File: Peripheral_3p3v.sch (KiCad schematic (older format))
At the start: 0 parts

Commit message: Lots of changes for MFG: parts info
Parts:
- added L3: 4.7uH, symbol Device:L
- added U8: TPS54202HDDCR, SmartBattery:SOT95P280X110-6N, symbol SmartBattery:TPS54202HDDCR
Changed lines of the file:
@@
 $Descr A4 11693 8268
 encoding utf-8
-Sheet 1 5
+Sheet 5 5
 Title ""
 Date ""
@@
 Comment4 ""
 $EndDescr
+$Comp
+L SmartBattery:TPS54202HDDCR U8
+U 1 1 5FE1C5BF
+P 3950 3400
+F 0 "U8" H 3950 3970 50  0000 C CNN
+F 1 "TPS54202HDDCR" H 3950 3879 50  0000 C CNN
+F 2 "SmartBattery:SOT95P280X110-6N" H 3950 3400 50  0001 L BNN
+F 3 "" H 3950 3400 50  0001 L BNN
+F 4 "TPS54202HDDCR" H 3950 3400 50  0001 C CNN "SKU"
+	1    3950 3400
+	1    0    0    -1
+$EndComp
+$Comp
+L Device:L L3
+U 1 1 5FE1E2B4
+P 6100 3350
+F 0 "L3" H 6153 3396 50  0000 L CNN
+F 1 "4.7uH" H 6153 3305 50  0000 L CNN
+F 2 "" H 6100 3350 50  0001 C CNN
+F 3 "~" H 6100 3350 50  0001 C CNN
+F 4 "303010114" H 6100 3350 50  0001 C CNN "SKU"
+	1    6100 3350
+	1    0    0    -1
+$EndComp
 $EndSCHEMATC

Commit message: Switching over to jlpcb
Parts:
- removed U8: TPS54202HDDCR, SmartBattery:SOT95P280X110-6N, symbol SmartBattery:TPS54202HDDCR
- added U8: LMR14030SDDAR, SmartBattery:NOPB, symbol SmartBattery:LMR14030SDDAR
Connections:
- net labels added: 3p3v, VSYS
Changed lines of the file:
@@
 $Descr A4 11693 8268
 encoding utf-8
-Sheet 5 5
+Sheet 5 6
 Title ""
 Date ""
@@
 Comment4 ""
 $EndDescr
-$Comp
-L SmartBattery:TPS54202HDDCR U8
-U 1 1 5FE1C5BF
-P 3950 3400
-F 0 "U8" H 3950 3970 50  0000 C CNN
-F 1 "TPS54202HDDCR" H 3950 3879 50  0000 C CNN
-F 2 "SmartBattery:SOT95P280X110-6N" H 3950 3400 50  0001 L BNN
-F 3 "" H 3950 3400 50  0001 L BNN
-F 4 "TPS54202HDDCR" H 3950 3400 50  0001 C CNN "SKU"
-	1    3950 3400
-	1    0    0    -1
-$EndComp
 $Comp
 L Device:L L3
@@
 	1    0    0    -1
 $EndComp
+$Comp
+L SmartBattery:LMR14030SDDAR U8
+U 1 1 60084A34
+P 3350 3250
+F 0 "U8" H 3350 3920 50  0000 C CNN
+F 1 "LMR14030SDDAR" H 3350 3829 50  0000 C CNN
+F 2 "SmartBattery:NOPB" H 3350 3250 50  0001 L BNN
+F 3 "" H 3350 3250 50  0001 L BNN
+F 4 "C182078" H 3350 3250 50  0001 C CNN "LCSC"
+	1    3350 3250
+	1    0    0    -1
+$EndComp
+Text HLabel 1600 1600 0    50   Input ~ 0
+VSYS
+Text HLabel 5650 1650 2    50   Output ~ 0
+3p3v
 $EndSCHEMATC

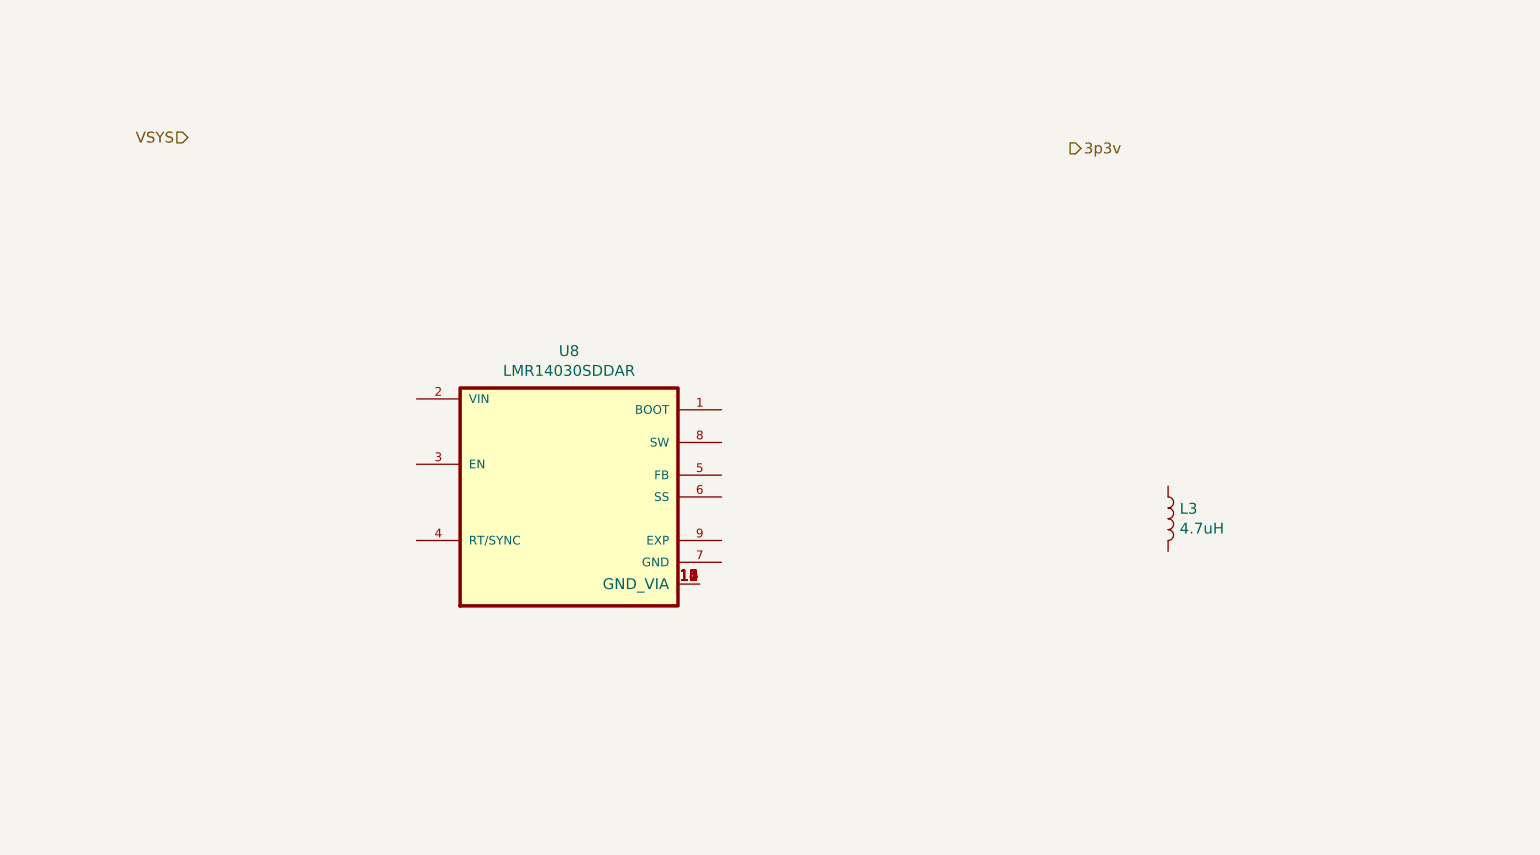
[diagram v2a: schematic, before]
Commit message: Replaced old charger to support JLC assembly. Very close now!
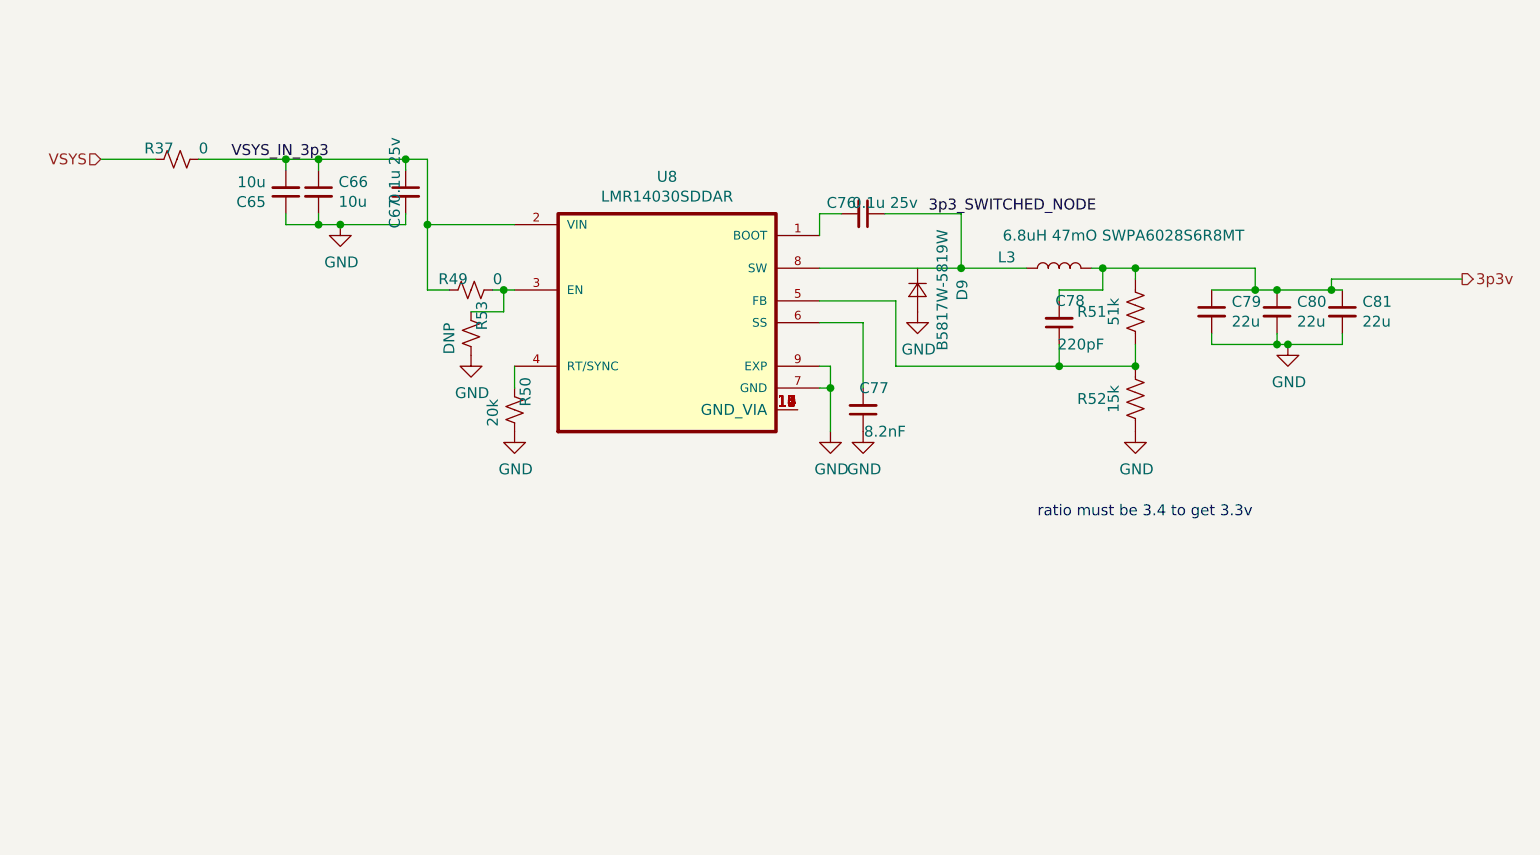
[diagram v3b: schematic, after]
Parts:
- added C65, C66: 10u, lc_lib:0805_C, symbol Device:C_Small
- added C67, C76: 0.1u 25v, lc_lib:0402_C, symbol Device:C_Small
- added C77: 8.2nF, lc_lib:0603_C, symbol Device:C_Small
- added C78: 220pF, lc_lib:0402_C, symbol Device:C_Small
- added C79, C80, C81: 22u, lc_lib:0805_C, symbol Device:C_Small
- added D9: B5817W-5819W, lc_lib:SOD-123, symbol Device:D_Small
- added R37, R49: 0, lc_lib:0402_R, symbol Device:R_Small_US
- added R50: 20k, lc_lib:0402_R, symbol Device:R_Small_US
- added R51: 51k, lc_lib:0402_R, symbol Device:R_US
- added R52: 15k, lc_lib:0402_R, symbol Device:R_US
- added R53: DNP, lc_lib:0402_R, symbol Device:R_Small_US
- L3: value 4.7uH -> 6.8uH 47mO SWPA6028S6R8MT; footprint (none) -> Inductor_SMD:L_Taiyo-Yuden_NR-60xx; SKU 303010114 -> (none); lcsc (none) -> C42261
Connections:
- net 3p3v: now also L3.2, C78.2, C79.1, C80.1, C81.1, R51.1
- net VSYS: now also R37.2
- net 3p3_SWITCHED_NODE: now reaches L3.1
- net 3p3_SWITCHED_NODE: now also U8.8 (SW), C76.1
- net at U8.1 (BOOT): now also C76.2
- net VSYS_IN_3p3: now reaches U8.2 (VIN)
- net VSYS_IN_3p3: now also C65.2, C66.1, C67.1, R37.1, R49.2
- net at U8.3 (EN): now also R49.1, R53.2
- net at U8.4 (RT/SYNC): now also R50.2
- net at U8.5 (FB): now also C78.1, R51.2, R52.1
- net at U8.6 (SS): now also C77.2
- net GND: now reaches U8.7 (GND)
- net GND: now also U8.9 (EXP), C65.1, C66.2, C67.2, C77.1, C79.2, C80.2, C81.2, D9.2 (A), R50.1, R52.2, R53.1
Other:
- note added: "ratio must be 3.4 to get 3.3v\n"
- moved on the sheet: L3, U8

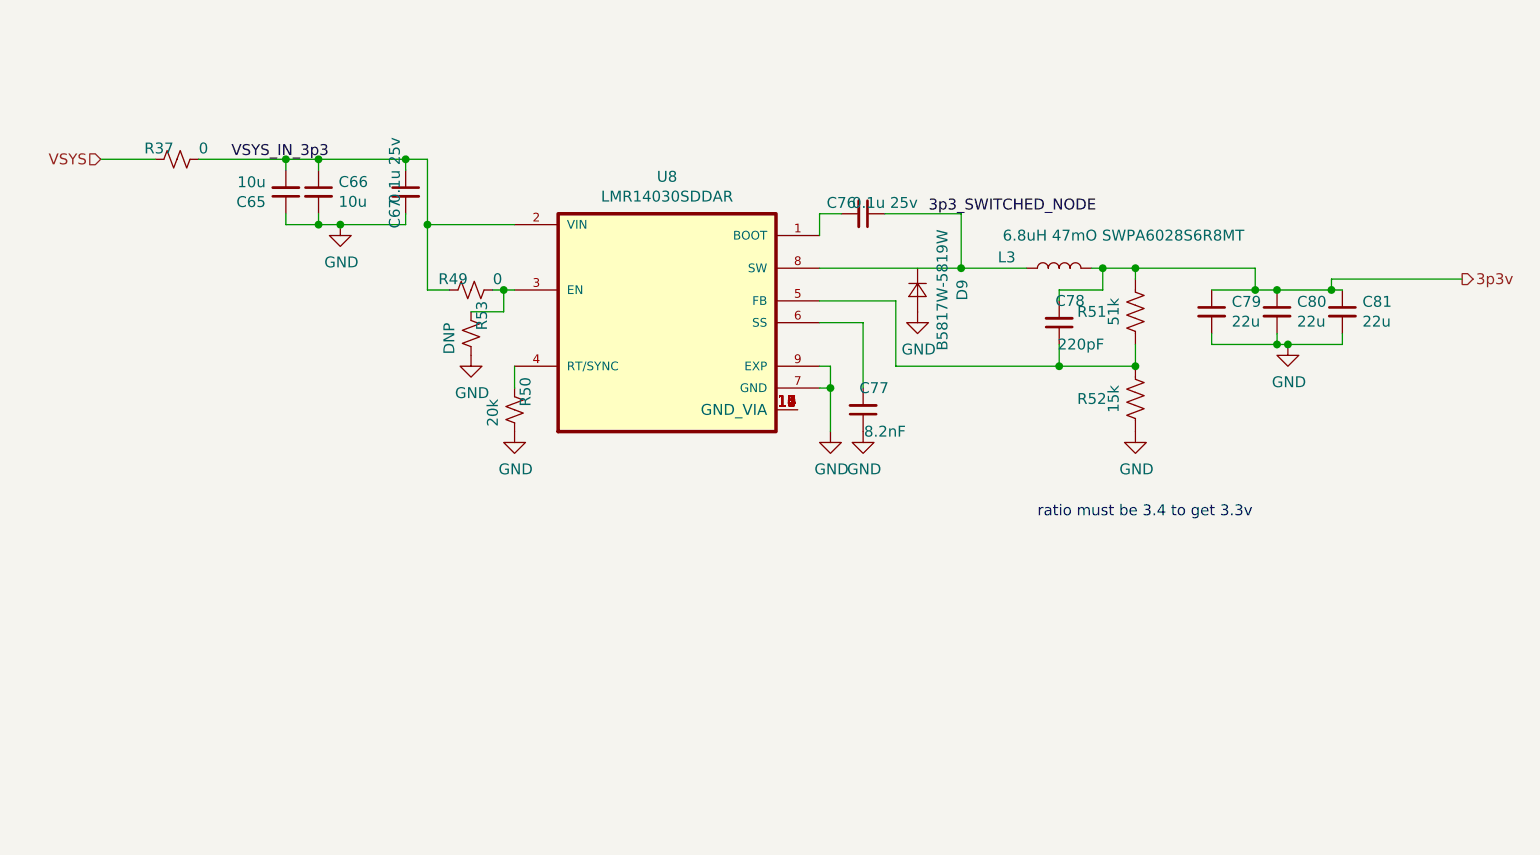
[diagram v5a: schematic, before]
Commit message: Type_A_implemented. Sch "locked". PCB Layout started.
*Changelog:
*Type-a switching regulator (TBD -- need to check inductor,caps, stability. Maybe check both peripherial inductors?)
*Type-A load switch + connector + esd
*started layout..
*found out that my footprint for n fet is wrong. Fixing now, need to replace all of those.
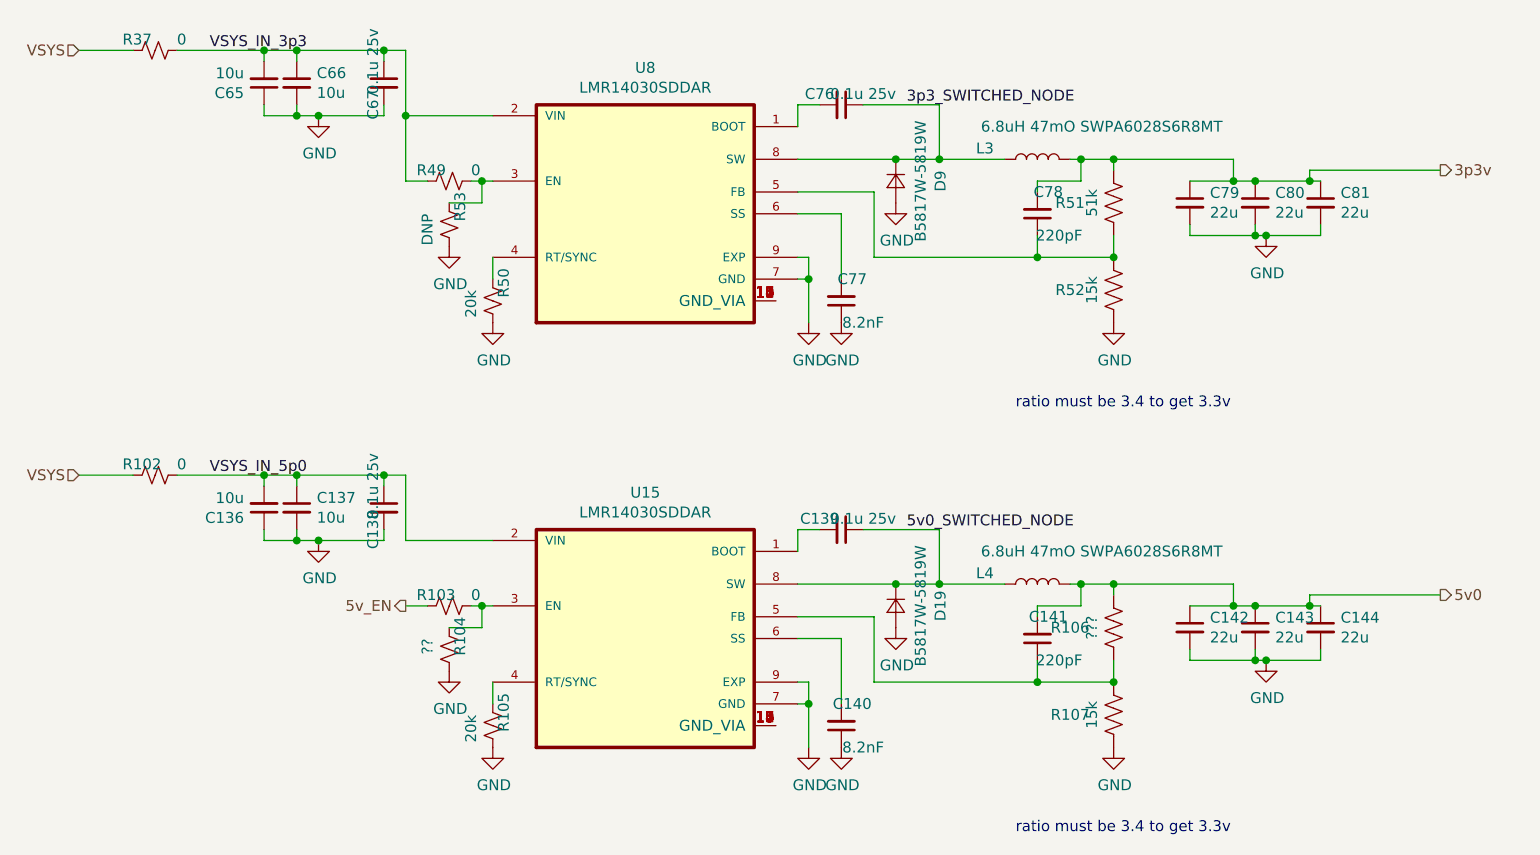
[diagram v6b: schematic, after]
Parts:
- added C136, C137: 10u, lc_lib:0805_C, symbol Device:C_Small
- added C138, C139: 0.1u 25v, lc_lib:0402_C, symbol Device:C_Small
- added C140: 8.2nF, lc_lib:0603_C, symbol Device:C_Small
- added C141: 220pF, lc_lib:0402_C, symbol Device:C_Small
- added C142, C143, C144: 22u, lc_lib:0805_C, symbol Device:C_Small
- added D19: B5817W-5819W, lc_lib:SOD-123, symbol Device:D_Small
- added L4: 6.8uH 47mO SWPA6028S6R8MT, Inductor_SMD:L_Taiyo-Yuden_NR-60xx, symbol Device:L
- added R102, R103: 0, lc_lib:0402_R, symbol Device:R_Small_US
- added R104: ??, lc_lib:0402_R, symbol Device:R_Small_US
- added R105: 20k, lc_lib:0402_R, symbol Device:R_Small_US
- added R106: ???, lc_lib:0402_R, symbol Device:R_US
- added R107: 15k, lc_lib:0402_R, symbol Device:R_US
- added U15: LMR14030SDDAR, SmartBattery:NOPB, symbol SmartBattery:LMR14030SDDAR
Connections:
- net 3p3_SWITCHED_NODE: now also D9.1 (K)
- net GND: now also C136.1, C137.2, C138.2, C140.1, C142.2, C143.2, C144.2, D19.2 (A), R104.1, R105.1, R107.2, U15.7 (GND), U15.9 (EXP)
- net VSYS: now also R102.2
- new net: C139.2, U15.1 (BOOT)
- new net: U15.10 (GND_VIA), U15.11 (GND_VIA), U15.12 (GND_VIA), U15.13 (GND_VIA), U15.14 (GND_VIA), U15.15 (GND_VIA), U15.16 (GND_VIA), U15.17 (GND_VIA)
- new net: R103.1, R104.2, U15.3 (EN)
- new net: R105.2, U15.4 (RT/SYNC)
- new net: C141.1, R106.2, R107.1, U15.5 (FB)
- new net: C140.2, U15.6 (SS)
- new net 5v0: C141.2, C142.1, C143.1, C144.1, L4.2, R106.1
- new net 5v0_SWITCHED_NODE: C139.1, D19.1 (K), L4.1, U15.8 (SW)
- new net 5v_EN: R103.2
- new net VSYS_IN_5p0: C136.2, C137.1, C138.1, R102.1, U15.2 (VIN)
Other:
- moved on the sheet: C65, C66, C67, C76, C77, C78, C79, C80, C81, D9, L3, R37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

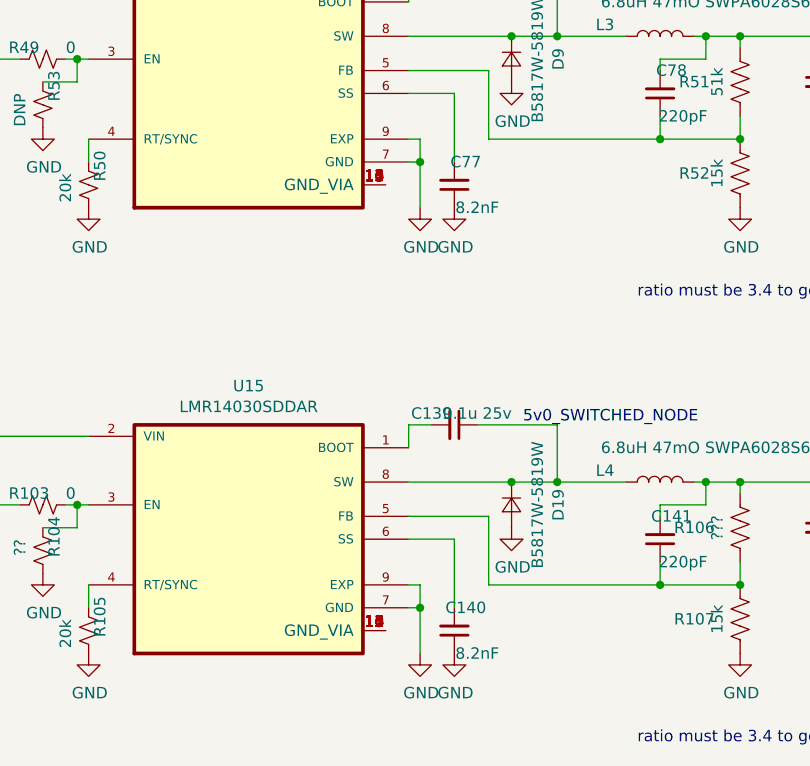
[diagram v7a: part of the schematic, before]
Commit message: Almost connected MCU + ESP32 added leds addedd uart usb cleaned up type-c I/O -- STILL NEED TO level shift I2C
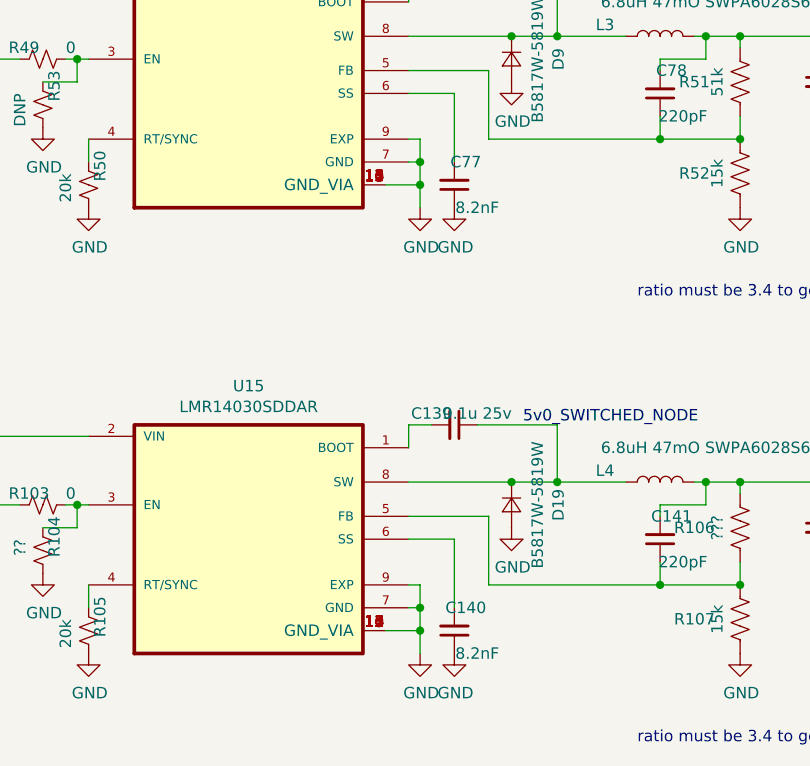
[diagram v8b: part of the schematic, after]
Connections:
- net GND: now also U15.10 (GND_VIA), U15.11 (GND_VIA), U15.12 (GND_VIA), U15.13 (GND_VIA), U15.14 (GND_VIA), U15.15 (GND_VIA), U15.16 (GND_VIA), U15.17 (GND_VIA), U8.10 (GND_VIA), U8.11 (GND_VIA), U8.12 (GND_VIA), U8.13 (GND_VIA), U8.14 (GND_VIA), U8.15 (GND_VIA), U8.16 (GND_VIA), U8.17 (GND_VIA)
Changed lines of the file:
@@
 	4400 2250 4450 2250
 Wire Wire Line
-	4450 2250 4450 2450
+	4450 2250 4450 2350
 Wire Wire Line
 	4400 2150 4450 2150
@@
 	4400 4200 4450 4200
 Wire Wire Line
-	4450 4200 4450 4400
+	4450 4200 4450 4300
 Wire Wire Line
 	4400 4100 4450 4100
@@
 Text HLabel 2600 3750 0    50   Output ~ 0
 5v_EN
+Wire Wire Line
+	4300 2350 4450 2350
+Connection ~ 4450 2350
+Wire Wire Line
+	4450 2350 4450 2450
+Wire Wire Line
+	4300 4300 4450 4300
+Connection ~ 4450 4300
+Wire Wire Line
+	4450 4300 4450 4400
 $EndSCHEMATC
